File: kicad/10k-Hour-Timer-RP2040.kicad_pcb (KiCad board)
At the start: 2 copper layers, 100 x 100 mm, 162 parts, among them J1 Conn_01x03_Pin, J10 S2B-PH-K-S_LF__SN_, J11 Conn_01x02_Pin, J2 JST_SH_SM03B, J3 USB_C_Receptacle_USB2.0_16P, J4 S2B-PH-K-S_LF__SN_, J5 Conn_02x05_Counter_Clockwise, J6 Conn_01x13_Pin, J7 Conn_01x03_Pin, J8 Conn_01x03_Pin, J9 Conn_01x02_Pin, Q1 PMOS, Q2 AO3400A, Q3 AO3400A, Q4 AO3400A, Q5 AO3400A, Q6 PMOS, SW2 BOOTSEL, SW3 RESET, SW4 USER_A, SW5 USER_B_PWR, SW6 SW_SPDT, U2 MCP73831-2-OT, U3 BQ29700DSER, U4 TLV62568DBVR, U5 W25Q128JVS, U6 RP2040, U7 PCF8523T, Y1 ABM8-272-T3, Y2 ABS07AIG-32.768KHZ-7-T

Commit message: floorplanning
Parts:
- moved J1 96.2 mm to (91.9, 46.5)
- moved J2 96.2 mm to (99.5, 49.0)
- moved J7 87.2 mm to (101.3, 60.8)
- moved TP20 50.1 mm to (58.3, 74.2)
- moved TP23 49.4 mm to (58.2, 69.5)
- moved J8 44.0 mm to (109.9, 71.5)
- moved C22 41.3 mm to (45.5, 81.8), turned to 0 degrees
- moved R42 39.3 mm to (63.3, 72.3), turned to 0 degrees
- moved D10 36.3 mm to (71.3, 79.4)
- moved JP23 36.2 mm to (65.1, 63.5), turned to 90 degrees
- moved J11 34.7 mm to (89.6, 87.9)
- moved JP13 34.7 mm to (91.2, 94.9)
- moved J10 34.7 mm to (96.0, 87.6)
- moved TP26 34.7 mm to (99.8, 94.2)
- moved R43 32.2 mm to (67.9, 72.3), turned to 180 degrees
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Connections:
- net /RTC/CLKOUT renamed /RTC/INT_CLKOUT
- D8 pad 2: /Power-DCDC-Charger-Battery/V_OUT -> 3V3

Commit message: layout - 7seg display
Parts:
- added H1: MH-4.7mm, project footprints:MountingHole_4.7mm, F.Cu at (19.8, 112.7)
- added H2: MH-4.7mm, project footprints:MountingHole_4.7mm, F.Cu at (113.0, 112.7)
- added H3: MH-4.7mm, project footprints:MountingHole_4.7mm, F.Cu at (113.0, 19.5)
- added H4: MH-4.7mm, project footprints:MountingHole_4.7mm, F.Cu at (19.8, 19.5)
- added R44: 10K, Resistor_SMD:R_0805_2012Metric_Pad1.20x1.40mm_HandSolder, F.Cu at (72.8, 113.5)
- added U8: FJ2481CH, project footprints:7-Seg-CC28-FJ2481CH, F.Cu at (82.5, 33.8)
- added U9: FJ2481CH, project footprints:7-Seg-CC28-FJ2481CH, F.Cu at (82.5, 45.3)
- R36: value 1K -> 10K
- moved D9 100.2 mm to (29.3, 112.2)
- moved R37 100.2 mm to (33.2, 112.2)
- moved SW2 89.4 mm to (107.1, 73.2)
- moved R3 87.7 mm to (17.6, 27.3), turned to -90 degrees
- moved D1 79.0 mm to (18.1, 33.4), turned to -90 degrees
- moved JP2 74.0 mm to (19.6, 37.0), turned to 90 degrees
- moved SW3 73.9 mm to (107.0, 82.0)
- moved C21 68.9 mm to (44.9, 104.8)
- moved R28 67.1 mm to (103.3, 86.7), turned to 180 degrees
- moved R36 63.0 mm to (48.2, 58.8), turned to -90 degrees
- moved BZ2 62.9 mm to (79.2, 110.3)
- moved Q5 57.1 mm to (48.9, 62.9), turned to -90 degrees
- moved TP17 57.0 mm to (23.2, 68.0)
- moved JP20 55.8 mm to (75.2, 101.0), turned to 90 degrees
- moved JP14 52.6 mm to (91.8, 97.0), turned to 180 degrees
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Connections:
- J6 pad 7: /MCU-IO/IO10 -> unconnected-(J6-Pin_7-Pad7)
- U6 pad 13: /MCU-IO/IO10 -> /MCU-IO/BZ1
- U6 pad 14: /MCU-IO/DISP_STB -> /MCU-IO/DISP_DIO
- U6 pad 16: /MCU-IO/DISP_DIO -> /MCU-IO/DISP_STB
- U6 pad 8: /MCU-IO/BZ1 -> unconnected-(U6-GPIO6-Pad8)
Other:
- board text added: "BUZ EN"
- board text added: "SWCLK"
- board text added: "SWDIO"
- board text removed: "PWR"

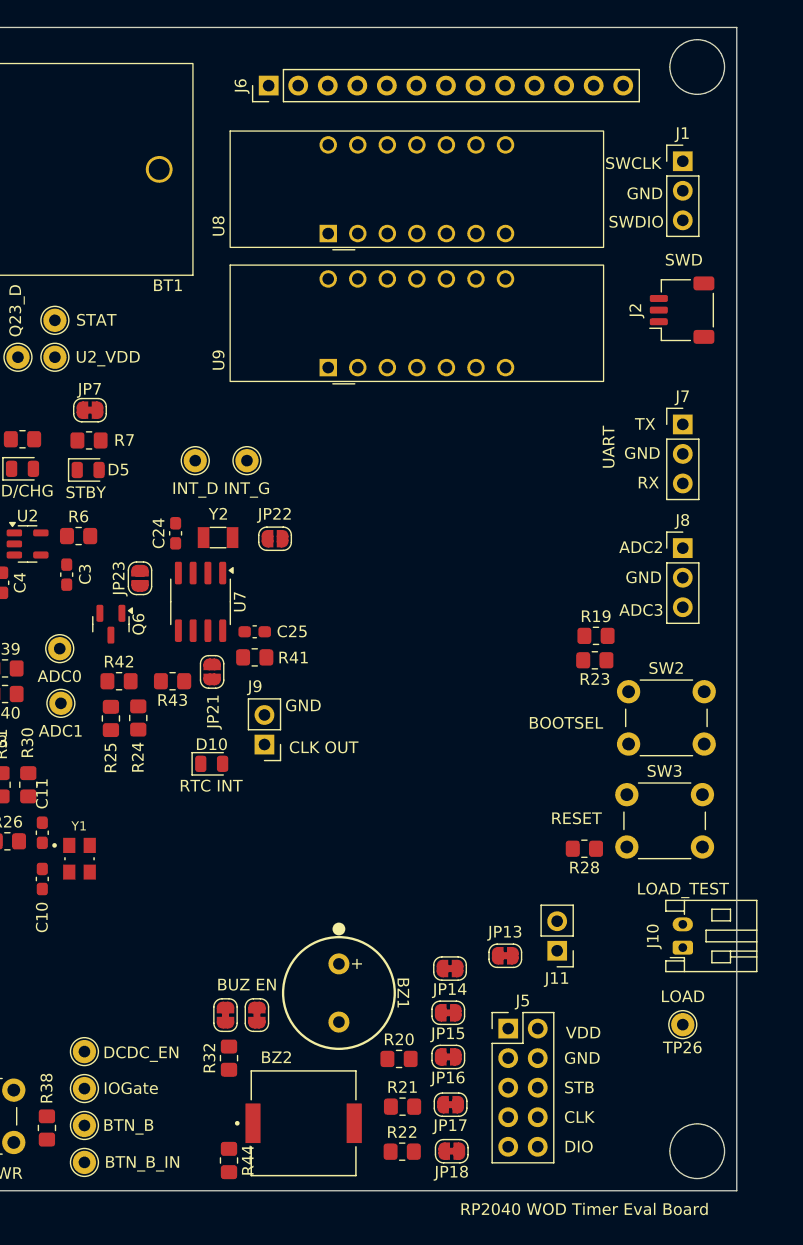
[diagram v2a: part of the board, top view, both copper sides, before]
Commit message: layout - footprints update - may have corrupted kicad_sch project lib
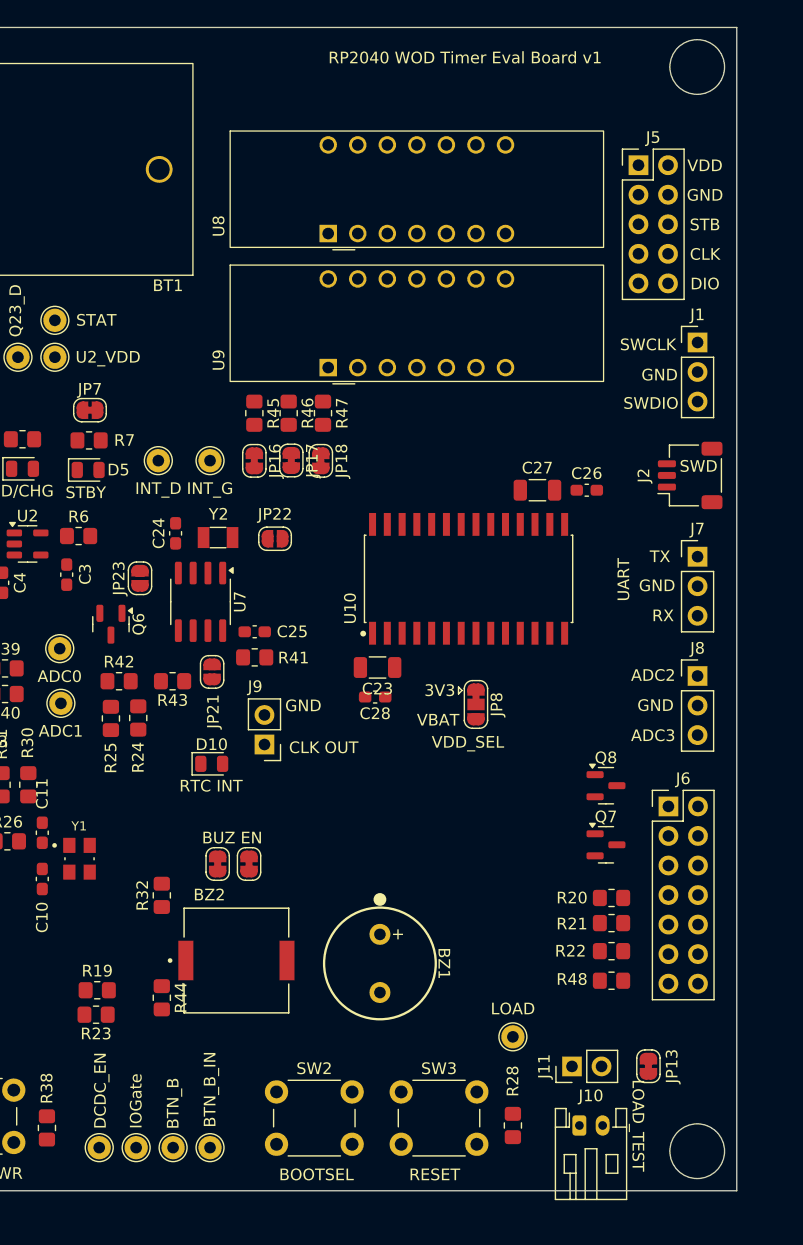
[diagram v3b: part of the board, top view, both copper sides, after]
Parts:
- removed JP14, JP15: SolderJumper_2_Bridged, Jumper:SolderJumper-2_P1.3mm_Bridged_RoundedPad1.0x1.5mm
- added C23: 100u, Capacitor_SMD:C_1206_3216Metric, F.Cu at (85.5, 71.1)
- added C26: 100n, Capacitor_SMD:C_0603_1608Metric_Pad1.08x0.95mm_HandSolder, F.Cu at (103.5, 55.9)
- added C27: 100u, Capacitor_SMD:C_1206_3216Metric, F.Cu at (99.3, 55.9)
- added C28: 100n, Capacitor_SMD:C_0603_1608Metric_Pad1.08x0.95mm_HandSolder, F.Cu at (85.3, 73.7)
- added JP8: SolderJumper_3_Bridged12, Jumper:SolderJumper-3_P1.3mm_Bridged12_RoundedPad1.0x1.5mm, F.Cu at (94.0, 74.3)
- added Q7: AO3400A, Package_TO_SOT_SMD:SOT-23, F.Cu at (105.2, 86.4)
- added Q8: AO3400A, Package_TO_SOT_SMD:SOT-23, F.Cu at (105.2, 81.3)
- added R45: 10K, Resistor_SMD:R_0805_2012Metric_Pad1.20x1.40mm_HandSolder, F.Cu at (74.9, 49.3)
- added R46: 10K, Resistor_SMD:R_0805_2012Metric_Pad1.20x1.40mm_HandSolder, F.Cu at (77.9, 49.3)
- added R47: 10K, Resistor_SMD:R_0805_2012Metric_Pad1.20x1.40mm_HandSolder, F.Cu at (80.8, 49.3)
- added R48: 10K, Resistor_SMD:R_0805_2012Metric_Pad1.20x1.40mm_HandSolder, F.Cu at (105.6, 98.0)
- added U10: TM1638, project footprints:SOIC127P1041X265-28N, F.Cu at (93.3, 63.5)
- J6: value Conn_01x13_Pin -> Conn_02x08_Counter_Clockwise; footprint Connector_PinHeader_2.54mm:PinHeader_1x13_P2.54mm_Vertical -> Connector_PinHeader_2.54mm:PinHeader_2x07_P2.54mm_Vertical
- R20, R22: value 10K -> 200
- moved J5 75.1 mm to (108.0, 27.9)
- moved J6 70.9 mm to (110.5, 83.1), turned to 0 degrees
- moved JP18 60.4 mm to (80.6, 53.4), turned to -90 degrees
- moved JP17 57.0 mm to (78.1, 53.3), turned to -90 degrees
- moved JP16 53.9 mm to (74.9, 53.4), turned to -90 degrees
- moved R23 52.6 mm to (61.3, 101.0)
- moved R19 52.6 mm to (61.4, 98.9)
- moved SW2 45.8 mm to (76.8, 107.6)
- moved SW3 32.1 mm to (87.6, 107.6)
- moved R22 24.9 mm to (105.6, 95.5)
- moved R28 24.6 mm to (97.2, 110.5), turned to 90 degrees
- moved R21 23.9 mm to (105.6, 93.1)
- moved R20 22.9 mm to (105.6, 90.9)
- moved J10 17.7 mm to (102.9, 110.5), turned to 0 degrees
- moved J1 15.6 mm to (113.0, 43.2)
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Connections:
- net /MCU-IO/CLK_Out renamed /TM1638_Display/CLK_Out
- net /MCU-IO/DIO_Out renamed /TM1638_Display/DIO_Out
- net /MCU-IO/STB_Out renamed /TM1638_Display/STB_Out
- net /MCU-IO/VDD_Out renamed /TM1638_Display/VDD_SEL
- net Vbatt_Vbus renamed /MCU-IO/VBAT_VBUS
- J5 pad 3: /MCU-IO/GND_Out -> GND
- J5 pad 4: /MCU-IO/GND_Out -> GND
- J6 pad 11: /MCU-IO/IO21 -> /MCU-IO/IO6
- J6 pad 12: /MCU-IO/IO22 -> /MCU-IO/IO21
- J6 pad 13: GND -> /MCU-IO/IO9
- J6 pad 2: /MCU-IO/IO2 -> 3V3
- J6 pad 3: /MCU-IO/IO3 -> 3V3
- J6 pad 4: /MCU-IO/IO4 -> /MCU-IO/IO3_LD-
- J6 pad 5: /MCU-IO/IO5 -> /MCU-IO/IO2_LD-
- J6 pad 6: /MCU-IO/IO9 -> /MCU-IO/IO14
- J6 pad 7: unconnected-(J6-Pin_7-Pad7) -> /MCU-IO/IO4
- J6 pad 8: /MCU-IO/IO14 -> /MCU-IO/IO15
- J6 pad 9: /MCU-IO/IO15 -> /MCU-IO/IO5
- R20 pad 1: 3V3 -> /MCU-IO/IO3
- R20 pad 2: /MCU-IO/DISP_STB -> Net-(Q8-G)
- R21 pad 1: 3V3 -> GND
- R21 pad 2: /MCU-IO/DISP_CLK -> Net-(Q8-G)
- R22 pad 1: 3V3 -> /MCU-IO/IO2
- R22 pad 2: /MCU-IO/DISP_DIO -> Net-(Q7-G)
- U6 pad 8: unconnected-(U6-GPIO6-Pad8) -> /MCU-IO/IO6
- U8 pad 1: unconnected-(U8-DIG1-Pad1) -> /TM1638_Display/Dig_1
- U8 pad 10: unconnected-(U8-g-Pad10) -> /TM1638_Display/SEG_G
- U8 pad 11: unconnected-(U8-DX-Pad11) -> /TM1638_Display/SEG_DX
- U8 pad 12: unconnected-(U8-DIG2-Pad12) -> /TM1638_Display/Dig_2
- U8 pad 13: unconnected-(U8-f-Pad13) -> /TM1638_Display/SEG_F
- U8 pad 14: unconnected-(U8-a-Pad14) -> /TM1638_Display/SEG_A
- U8 pad 2: Net-(U8-NA) -> /TM1638_Display/SEG_D
- U8 pad 3: unconnected-(U8-DPX-Pad3) -> /TM1638_Display/SEG_DPX
- U8 pad 4: unconnected-(U8-e-Pad4) -> /TM1638_Display/SEG_E
- U8 pad 5: unconnected-(U8-DIG3-Pad5) -> /TM1638_Display/Dig_3
- U8 pad 6: unconnected-(U8-c-Pad6) -> /TM1638_Display/SEG_C
- U8 pad 7: Net-(U8-NA) -> /TM1638_Display/SEG_D
- U8 pad 8: unconnected-(U8-b-Pad8) -> /TM1638_Display/SEG_B
- U8 pad 9: unconnected-(U8-DIG4-Pad9) -> /TM1638_Display/Dig_4
- U9 pad 1: unconnected-(U9-DIG1-Pad1) -> /TM1638_Display/Dig_5
- U9 pad 10: unconnected-(U9-g-Pad10) -> /TM1638_Display/SEG_G
- U9 pad 11: unconnected-(U9-DX-Pad11) -> /TM1638_Display/SEG_DX
- U9 pad 12: unconnected-(U9-DIG2-Pad12) -> /TM1638_Display/Dig_6
- U9 pad 13: unconnected-(U9-f-Pad13) -> /TM1638_Display/SEG_F
- U9 pad 14: unconnected-(U9-a-Pad14) -> /TM1638_Display/SEG_A
- U9 pad 2: Net-(U9-NA) -> /TM1638_Display/SEG_D
- U9 pad 3: unconnected-(U9-DPX-Pad3) -> /TM1638_Display/SEG_DPX
- U9 pad 4: unconnected-(U9-e-Pad4) -> /TM1638_Display/SEG_E
- U9 pad 5: unconnected-(U9-DIG3-Pad5) -> /TM1638_Display/Dig_7
- U9 pad 6: unconnected-(U9-c-Pad6) -> /TM1638_Display/SEG_C
- U9 pad 7: Net-(U9-NA) -> /TM1638_Display/SEG_D
- U9 pad 8: unconnected-(U9-b-Pad8) -> /TM1638_Display/SEG_B
- U9 pad 9: unconnected-(U9-DIG4-Pad9) -> /TM1638_Display/Dig_8
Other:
- board text added: "3V3"
- board text added: "RP2040 WOD Timer Eval Board v1"
- board text added: "VBAT"
- board text added: "VDD_SEL"
- board text removed: "RP2040 WOD Timer Eval Board"

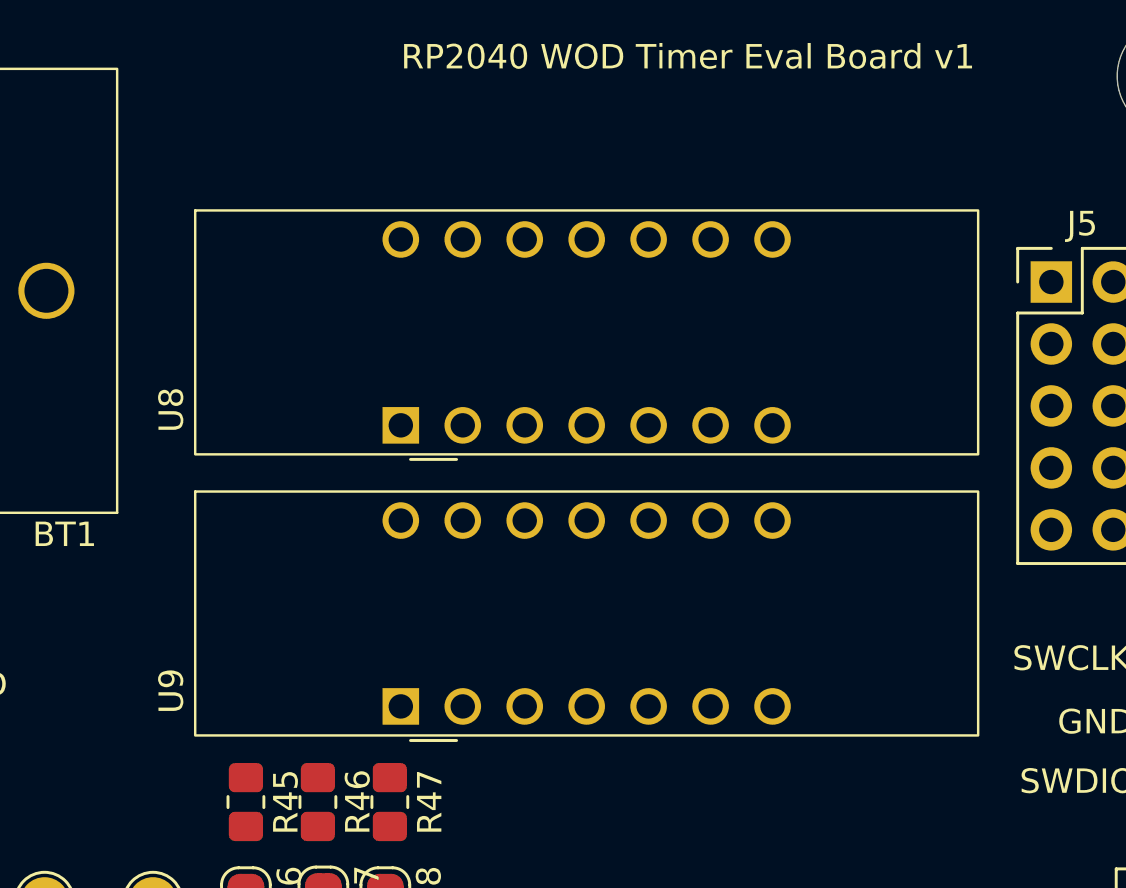
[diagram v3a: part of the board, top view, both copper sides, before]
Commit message: floorplanning - fixed 7seg symbol issue
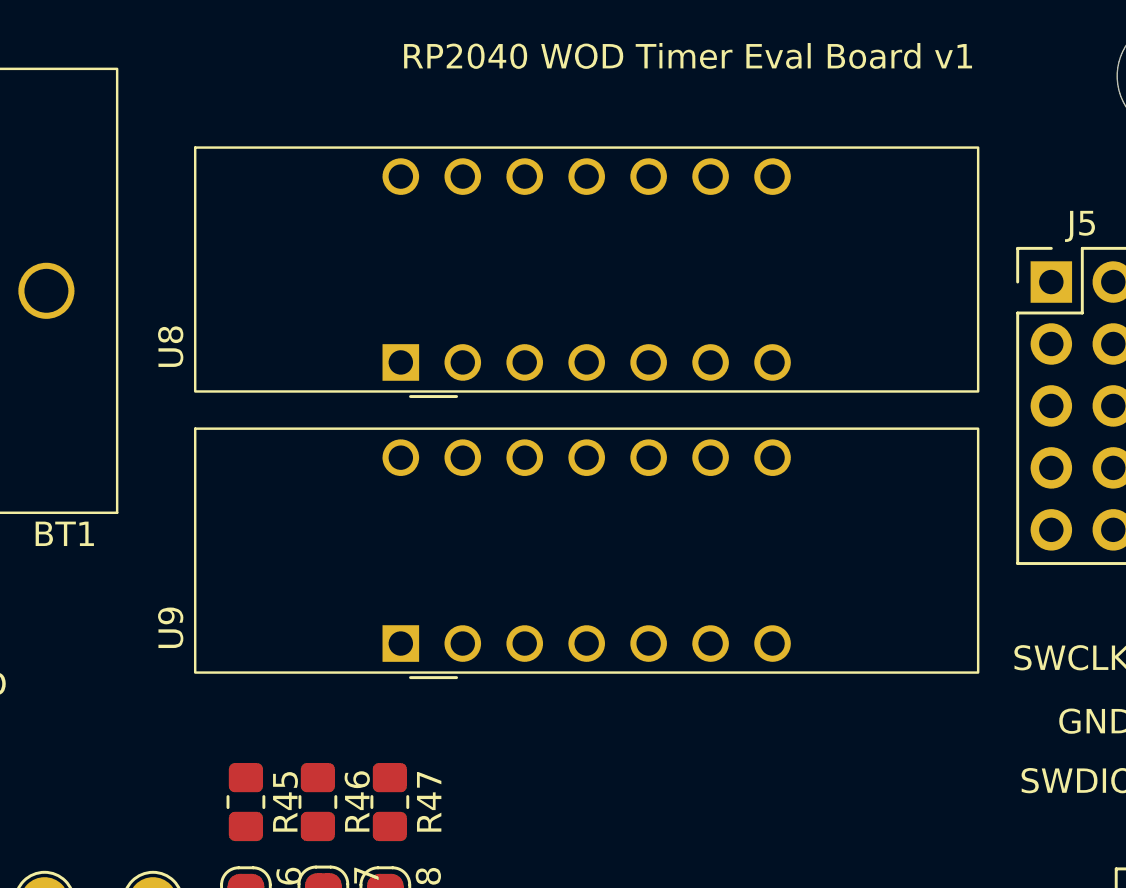
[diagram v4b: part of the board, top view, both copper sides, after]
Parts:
- moved U8 2.58 mm to (82.5, 31.2)
- moved U9 2.58 mm to (82.5, 42.8)
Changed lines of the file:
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@@
 	(footprint "project footprints:7-Seg-CC28-FJ2481CH"
 		(layer "F.Cu")
-		(at 82.55 33.815)
+		(at 82.55 31.237)
 		(descr "4 digit 7 segment LED 0.28inch digits")
 		(tags "4 digit 7 segment ")
@@
 			(layer "User.2")
 			(pts
-				(xy 104.95 35.005) (xy 104.95 25.005)
+				(xy 104.95 32.427) (xy 104.95 22.427)
 			)
 			(height 3.1)
@@
 			)
 			(gr_text "10"
-				(at 106.9 30.005 90)
+				(at 106.9 27.427 90)
 				(layer "User.2")
 				(effects
@@
 			(layer "User.2")
 			(pts
-				(xy 110.03 25.005) (xy 77.93 25.005)
+				(xy 110.03 22.427) (xy 77.93 22.427)
 			)
 			(height -5.69)
@@
 			)
 			(gr_text "32.1"
-				(at 93.98 18.165 0)
+				(at 93.98 15.587 0)
 				(layer "User.2")
 				(effects
@@
 			(layer "User.2")
 			(pts
-				(xy 72.85 35.005) (xy 82.55 33.815)
+				(xy 72.85 32.427) (xy 82.55 31.237)
 			)
 			(height -2.3)
@@
 			)
 			(gr_text "1.19"
-				(at 69.4 34.41 90)
+				(at 69.4 31.832 90)
 				(layer "User.2")
 				(effects
@@
 			(layer "User.2")
 			(pts
-				(xy 95.25 26.195) (xy 95.25 33.815)
+				(xy 95.25 23.617) (xy 95.25 31.237)
 			)
 			(height 3.8)
@@
 			)
 			(gr_text "7.62"
-				(at 97.9 30.005 90)
+				(at 97.9 27.427 90)
 				(layer "User.2")
 				(effects
@@
 			(layer "User.2")
 			(pts
-				(xy 95.25 26.195) (xy 104.95 25.005)
+				(xy 95.25 23.617) (xy 104.95 22.427)
 			)
 			(height 17.8)
@@
 			)
 			(gr_text "1.19"
-				(at 111.9 25.6 90)
+				(at 111.9 23.022 90)
 				(layer "User.2")
 				(effects
@@
 	(footprint "project footprints:7-Seg-CC28-FJ2481CH"
 		(layer "F.Cu")
-		(at 82.55 45.339)
+		(at 82.55 42.761)
 		(descr "4 digit 7 segment LED 0.28inch digits")
 		(tags "4 digit 7 segment ")
@@
 			(layer "User.2")
 			(pts
-				(xy 95.25 37.719) (xy 104.95 36.529)
+				(xy 95.25 35.141) (xy 104.95 33.951)
 			)
 			(height 17.8)
@@
 			)
 			(gr_text "1.19"
-				(at 111.9 37.124 90)
+				(at 111.9 34.546 90)
 				(layer "User.2")
 				(effects
@@
 			(layer "User.2")
 			(pts
-				(xy 72.85 46.529) (xy 82.55 45.339)
+				(xy 72.85 43.951) (xy 82.55 42.761)
 			)
 			(height -2.3)
@@
 			)
 			(gr_text "1.19"
-				(at 69.4 45.934 90)
+				(at 69.4 43.356 90)
 				(layer "User.2")
 				(effects
@@
 			(layer "User.2")
 			(pts
-				(xy 110.03 36.529) (xy 77.93 36.529)
+				(xy 110.03 33.951) (xy 77.93 33.951)
 			)
 			(height -5.69)
@@
 			)
 			(gr_text "32.1"
-				(at 93.98 29.689 0)
+				(at 93.98 27.111 0)
 				(layer "User.2")
 				(effects
@@
 			(layer "User.2")
 			(pts
-				(xy 95.25 37.719) (xy 95.25 45.339)
+				(xy 95.25 35.141) (xy 95.25 42.761)
 			)
 			(height 3.8)
@@
 			)
 			(gr_text "7.62"
-				(at 97.9 41.529 90)
+				(at 97.9 38.951 90)
 				(layer "User.2")
 				(effects
@@
 			(layer "User.2")
 			(pts
-				(xy 104.95 46.529) (xy 104.95 36.529)
+				(xy 104.95 43.951) (xy 104.95 33.951)
 			)
 			(height 3.1)
@@
 			)
 			(gr_text "10"
-				(at 106.9 41.529 90)
+				(at 106.9 38.951 90)
 				(layer "User.2")
 				(effects
